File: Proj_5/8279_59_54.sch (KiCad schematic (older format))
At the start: 40 parts, among them SW10 Switch_SW_SPST, SW11 Switch_SW_SPST, SW12 Switch_SW_SPST, SW13 Switch_SW_SPST, SW14 Switch_SW_SPST, SW15 Switch_SW_SPST, SW16 Switch_SW_SPST, SW17 Switch_SW_SPST, SW18 Switch_SW_SPST, SW19 Switch_SW_SPST, SW2 Shift, SW20 Switch_SW_SPST, SW21 Switch_SW_SPST, SW22 Switch_SW_SPST, SW23 Switch_SW_SPST, SW3 Switch_SW_SPST, SW4 Switch_SW_SPST, SW5 Switch_SW_SPST, SW6 Switch_SW_SPST, SW7 CTRL, SW8 Switch_SW_SPST, SW9 Switch_SW_SPST, U10 8259, U11 8254, U17 pkd8279, U18 74LS138

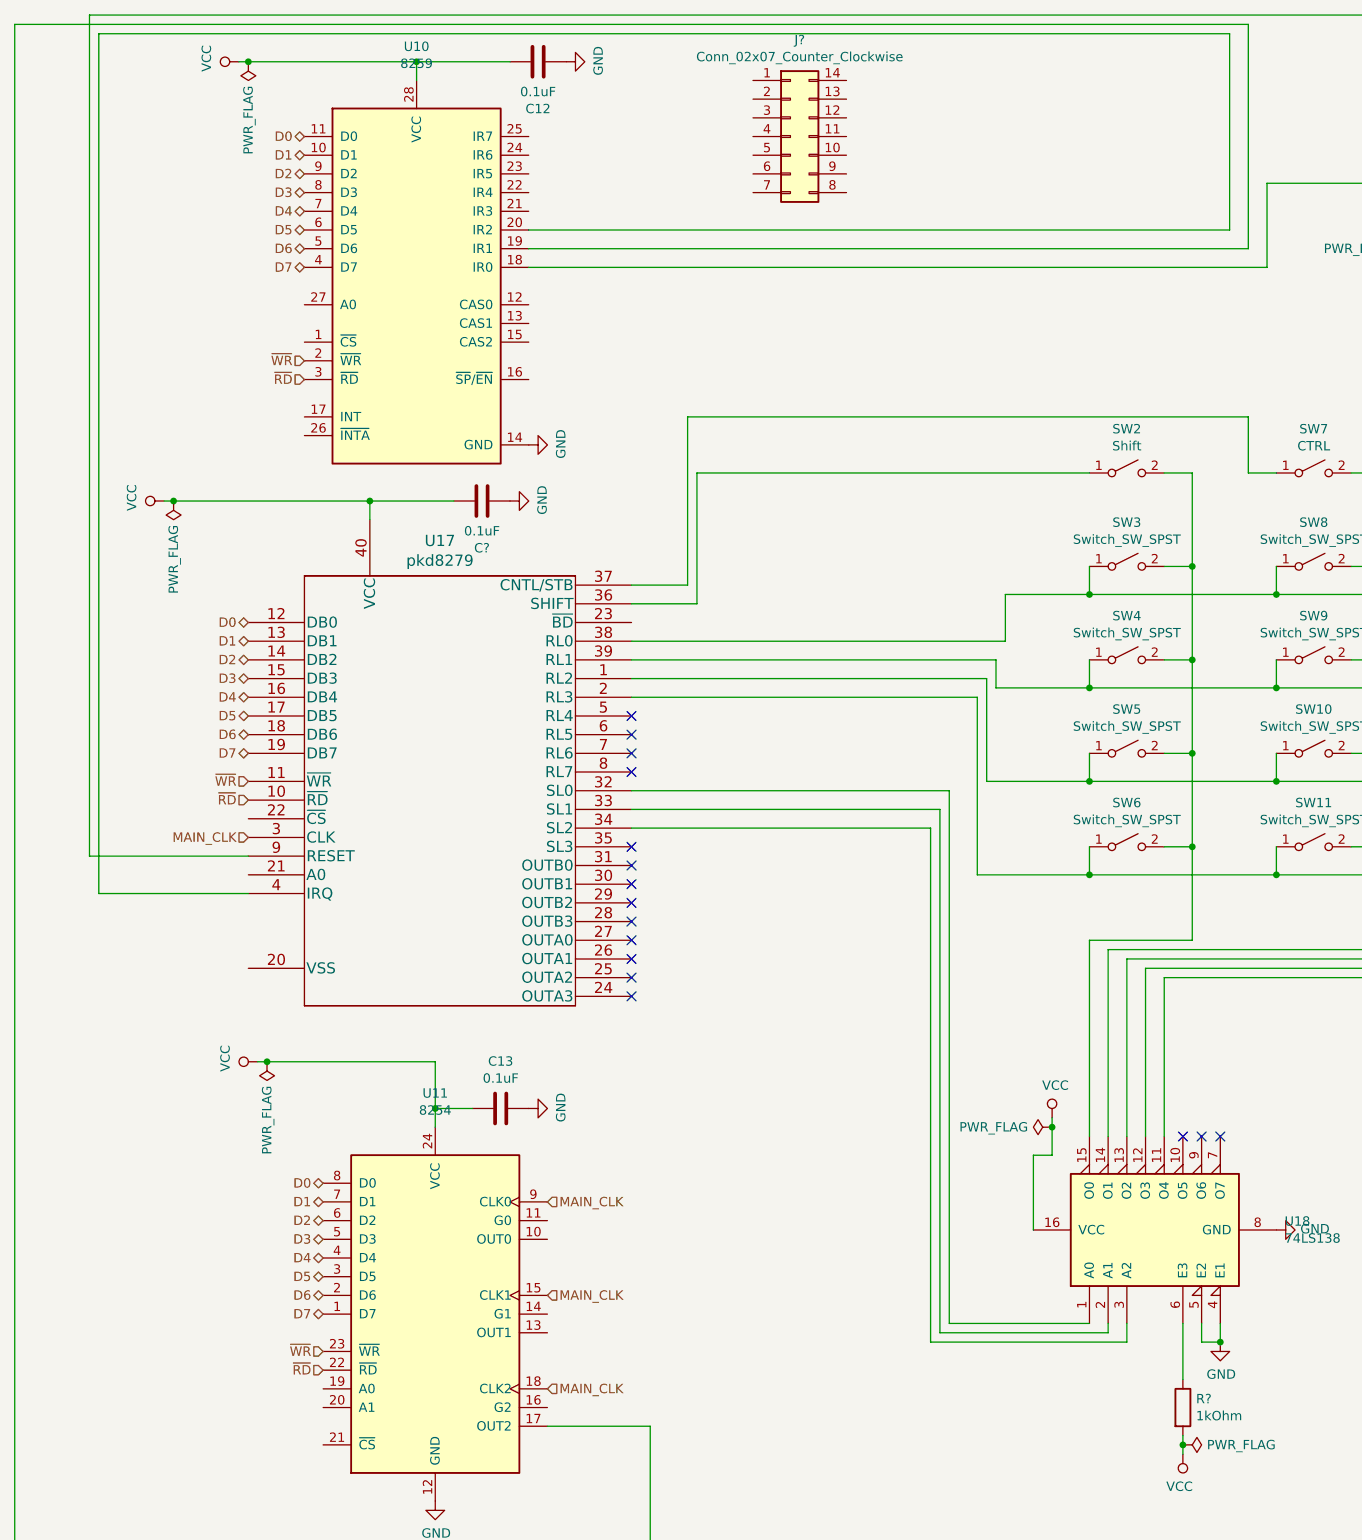
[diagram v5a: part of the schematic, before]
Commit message: Rerouted Ext Wires, UART Mostly Complete, All Headers Added
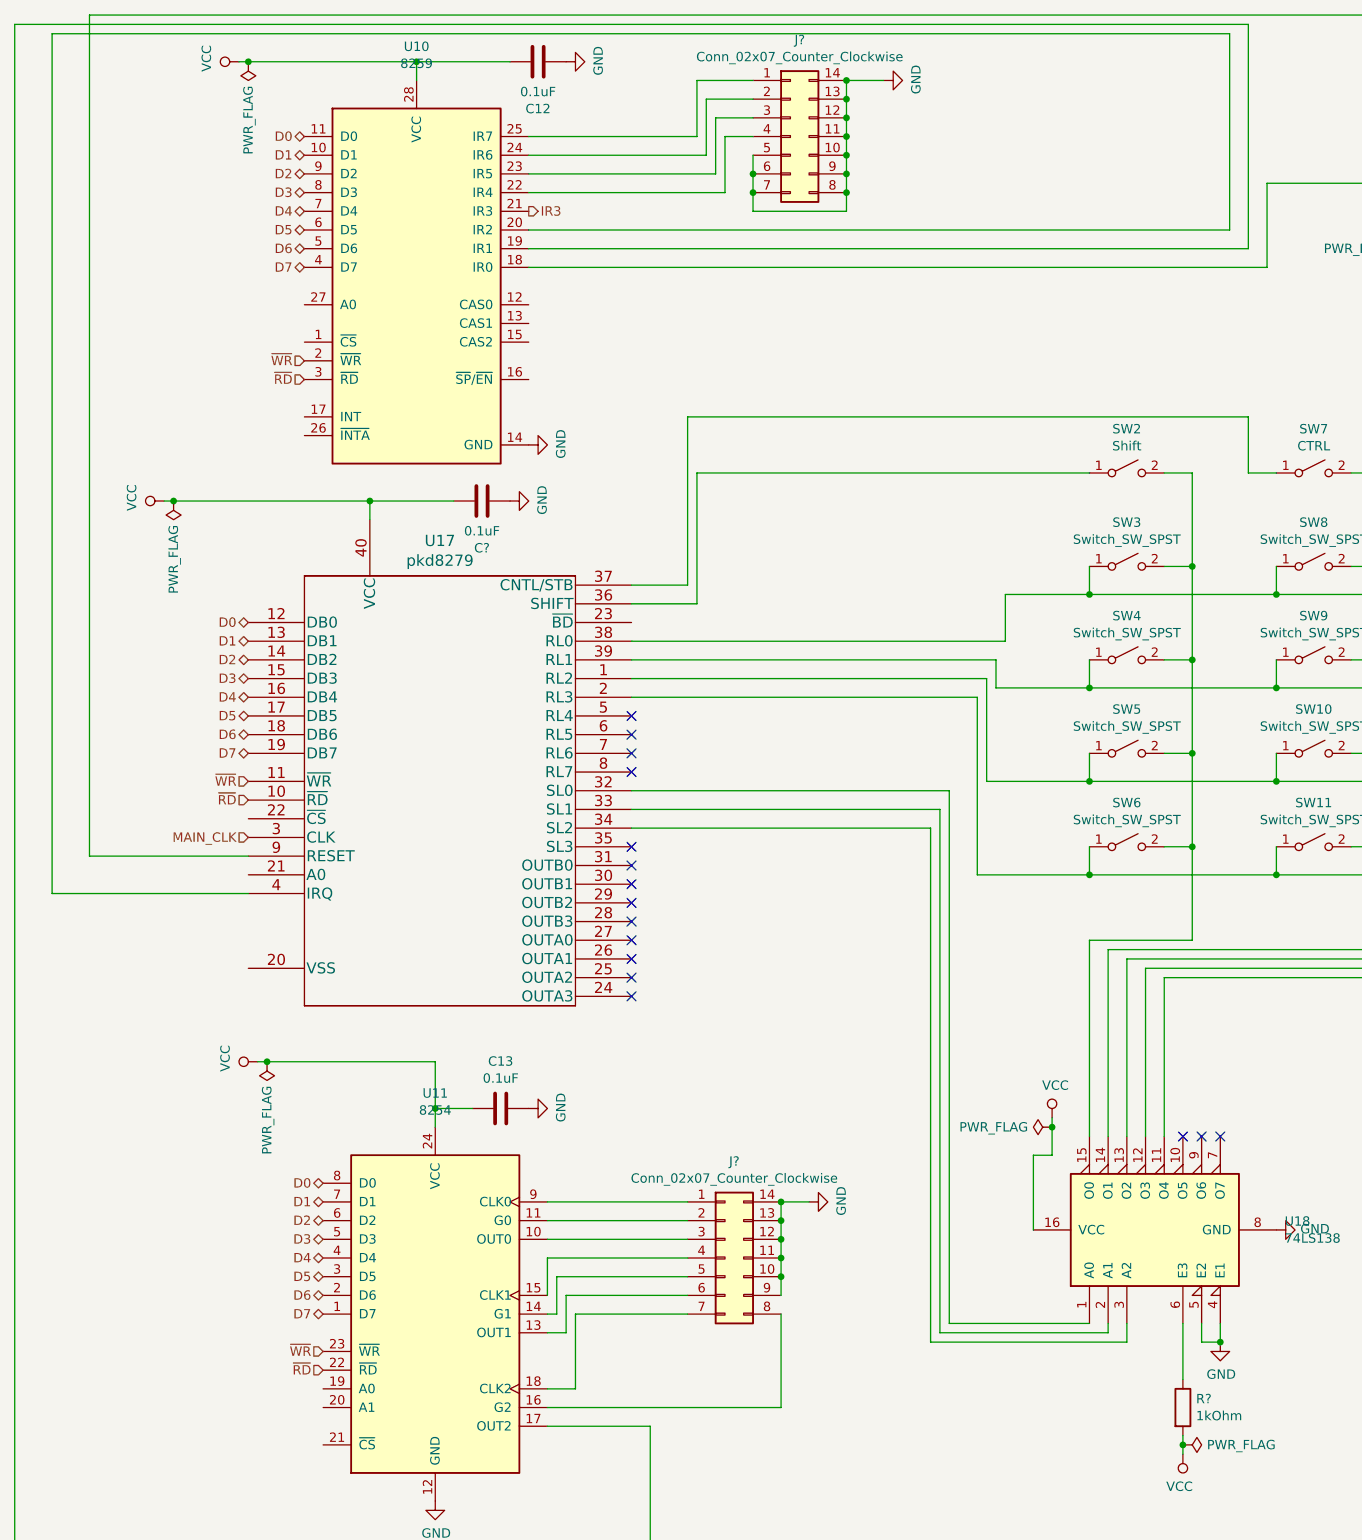
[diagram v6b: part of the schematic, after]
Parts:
- added J?: Conn_02x07_Counter_Clockwise, symbol Connector_Generic:Conn_02x07_Counter_Clockwise
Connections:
- net GND: now also J?.10 (Pin_10), J?.11 (Pin_11), J?.12 (Pin_12), J?.13 (Pin_13), J?.14 (Pin_14), J?.5 (Pin_5), J?.6 (Pin_6), J?.7 (Pin_7), J?.8 (Pin_8), J?.9 (Pin_9), J?.10 (Pin_10), J?.11 (Pin_11), J?.12 (Pin_12), J?.13 (Pin_13), J?.14 (Pin_14), J?.9 (Pin_9)
- net MAIN_CLK: no longer U11.15 (CLK1), U11.18 (CLK2), U11.9 (CLK0)
- net at U11.10 (OUT0): now also J?.3 (Pin_3)
- net at U11.11 (G0): now also J?.2 (Pin_2)
- net at U11.13 (OUT1): now also J?.6 (Pin_6)
- net at U11.14 (G1): now also J?.5 (Pin_5)
- net at U11.16 (G2): now also J?.8 (Pin_8)
- net IR3: now reaches U10.21 (IR3)
- net at U10.22 (IR4): now also J?.4 (Pin_4)
- net at U10.23 (IR5): now also J?.3 (Pin_3)
- net at U10.24 (IR6): now also J?.2 (Pin_2)
- net at U10.25 (IR7): now also J?.1 (Pin_1)
- new net: J?.4 (Pin_4), U11.15 (CLK1)
- new net: J?.7 (Pin_7), U11.18 (CLK2)
- new net: J?.1 (Pin_1), U11.9 (CLK0)
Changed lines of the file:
@@
 $Descr A2 23386 16535
 encoding utf-8
-Sheet 8 9
+Sheet 7 9
 Title ""
 Date ""
@@
 Wire Wire Line
 	11000 1900 7050 1900
-Text HLabel 7150 6900 2    50   Input ~ 0
-MAIN_CLK
 Wire Wire Line
 	15550 1800 15550 1450
@@
 Text HLabel 5550 4950 0    50   Input ~ 0
 MAIN_CLK
-Text HLabel 7150 7400 2    50   Input ~ 0
-MAIN_CLK
-Text HLabel 7150 7900 2    50   Input ~ 0
-MAIN_CLK
 Text HLabel 5850 2400 0    50   Input ~ 0
 ~WR
@@
 	10900 600  10900 1800
 Wire Wire Line
-	4700 550  4700 5050
-Wire Wire Line
 	7050 1700 10800 1700
 Wire Wire Line
 	10800 1700 10800 650
-Wire Wire Line
-	10800 650  4750 650
-Wire Wire Line
-	4750 650  4750 5250
-Wire Wire Line
-	4750 5250 5550 5250
 Wire Wire Line
 	7600 4700 9300 4700
@@
 	1    0    0    -1
 $EndComp
+Text HLabel 7050 1600 2    50   Output ~ 0
+IR3
+Wire Wire Line
+	7050 1200 7950 1200
+Wire Wire Line
+	7950 1200 7950 900
+Wire Wire Line
+	7950 900  8250 900
+Wire Wire Line
+	7050 1300 8000 1300
+Wire Wire Line
+	8000 1300 8000 1000
+Wire Wire Line
+	8000 1000 8250 1000
+Wire Wire Line
+	7050 1400 8050 1400
+Wire Wire Line
+	8050 1400 8050 1100
+Wire Wire Line
+	8050 1100 8250 1100
+Wire Wire Line
+	7050 1500 8100 1500
+Wire Wire Line
+	8100 1500 8100 1200
+Wire Wire Line
+	8100 1200 8250 1200
+Wire Wire Line
+	8250 1300 8250 1400
+Wire Wire Line
+	8250 1400 8250 1500
+Connection ~ 8250 1400
+Wire Wire Line
+	8250 1500 8250 1600
+Wire Wire Line
+	8250 1600 8750 1600
+Wire Wire Line
+	8750 1600 8750 1500
+Connection ~ 8250 1500
+Connection ~ 8750 1000
+Wire Wire Line
+	8750 1000 8750 900
+Connection ~ 8750 1100
+Wire Wire Line
+	8750 1100 8750 1000
+Connection ~ 8750 1200
+Wire Wire Line
+	8750 1200 8750 1100
+Connection ~ 8750 1300
+Wire Wire Line
+	8750 1300 8750 1200
+Connection ~ 8750 1400
+Wire Wire Line
+	8750 1400 8750 1300
+Connection ~ 8750 1500
+Wire Wire Line
+	8750 1500 8750 1400
+Wire Wire Line
+	8750 900  8950 900
+Connection ~ 8750 900
+$Comp
+L power:GND #PWR?
+U 1 1 5F5C47E7
+P 8950 900
+F 0 "#PWR?" H 8950 650 50  0001 C CNN
+F 1 "GND" H 8955 727 50  0000 C CNN
+F 2 "" H 8950 900 50  0001 C CNN
+F 3 "" H 8950 900 50  0001 C CNN
+	1    8950 900
+	0    -1   -1   0
+$EndComp
+Wire Wire Line
+	4500 650  10800 650
+Wire Wire Line
+	4700 550  4700 5050
+Wire Wire Line
+	4500 650  4500 5250
+Wire Wire Line
+	4500 5250 5550 5250
+$Comp
+L Connector_Generic:Conn_02x07_Counter_Clockwise J?
+U 1 1 5F62591A
+P 8100 7200
+F 0 "J?" H 8150 7717 50  0000 C CNN
+F 1 "Conn_02x07_Counter_Clockwise" H 8150 7626 50  0000 C CNN
+F 2 "" H 8100 7200 50  0001 C CNN
+F 3 "~" H 8100 7200 50  0001 C CNN
+	1    8100 7200
+	1    0    0    -1
+$EndComp
+Wire Wire Line
+	7150 6900 7900 6900
+Wire Wire Line
+	7150 7000 7900 7000
+Wire Wire Line
+	7150 7100 7900 7100
+Wire Wire Line
+	7150 7400 7150 7200
+Wire Wire Line
+	7150 7200 7900 7200
+Wire Wire Line
+	7150 7500 7200 7500
+Wire Wire Line
+	7200 7500 7200 7300
+Wire Wire Line
+	7200 7300 7900 7300
+Wire Wire Line
+	7150 7600 7250 7600
+Wire Wire Line
+	7250 7600 7250 7400
+Wire Wire Line
+	7250 7400 7900 7400
+Wire Wire Line
+	7150 7900 7300 7900
+Wire Wire Line
+	7300 7900 7300 7500
+Wire Wire Line
+	7300 7500 7900 7500
+Wire Wire Line
+	7150 8000 8400 8000
+Wire Wire Line
+	8400 8000 8400 7500
+Wire Wire Line
+	8400 7400 8400 7300
+Connection ~ 8400 7000
+Wire Wire Line
+	8400 7000 8400 6900
+Connection ~ 8400 7100
+Wire Wire Line
+	8400 7100 8400 7000
+Connection ~ 8400 7200
+Wire Wire Line
+	8400 7200 8400 7100
+Connection ~ 8400 7300
+Wire Wire Line
+	8400 7300 8400 7200
+Wire Wire Line
+	8400 6900 8550 6900
+Connection ~ 8400 6900
+$Comp
+L power:GND #PWR?
+U 1 1 5F6F628E
+P 8550 6900
+F 0 "#PWR?" H 8550 6650 50  0001 C CNN
+F 1 "GND" H 8555 6727 50  0000 C CNN
+F 2 "" H 8550 6900 50  0001 C CNN
+F 3 "" H 8550 6900 50  0001 C CNN
+	1    8550 6900
+	0    -1   -1   0
+$EndComp
 $EndSCHEMATC

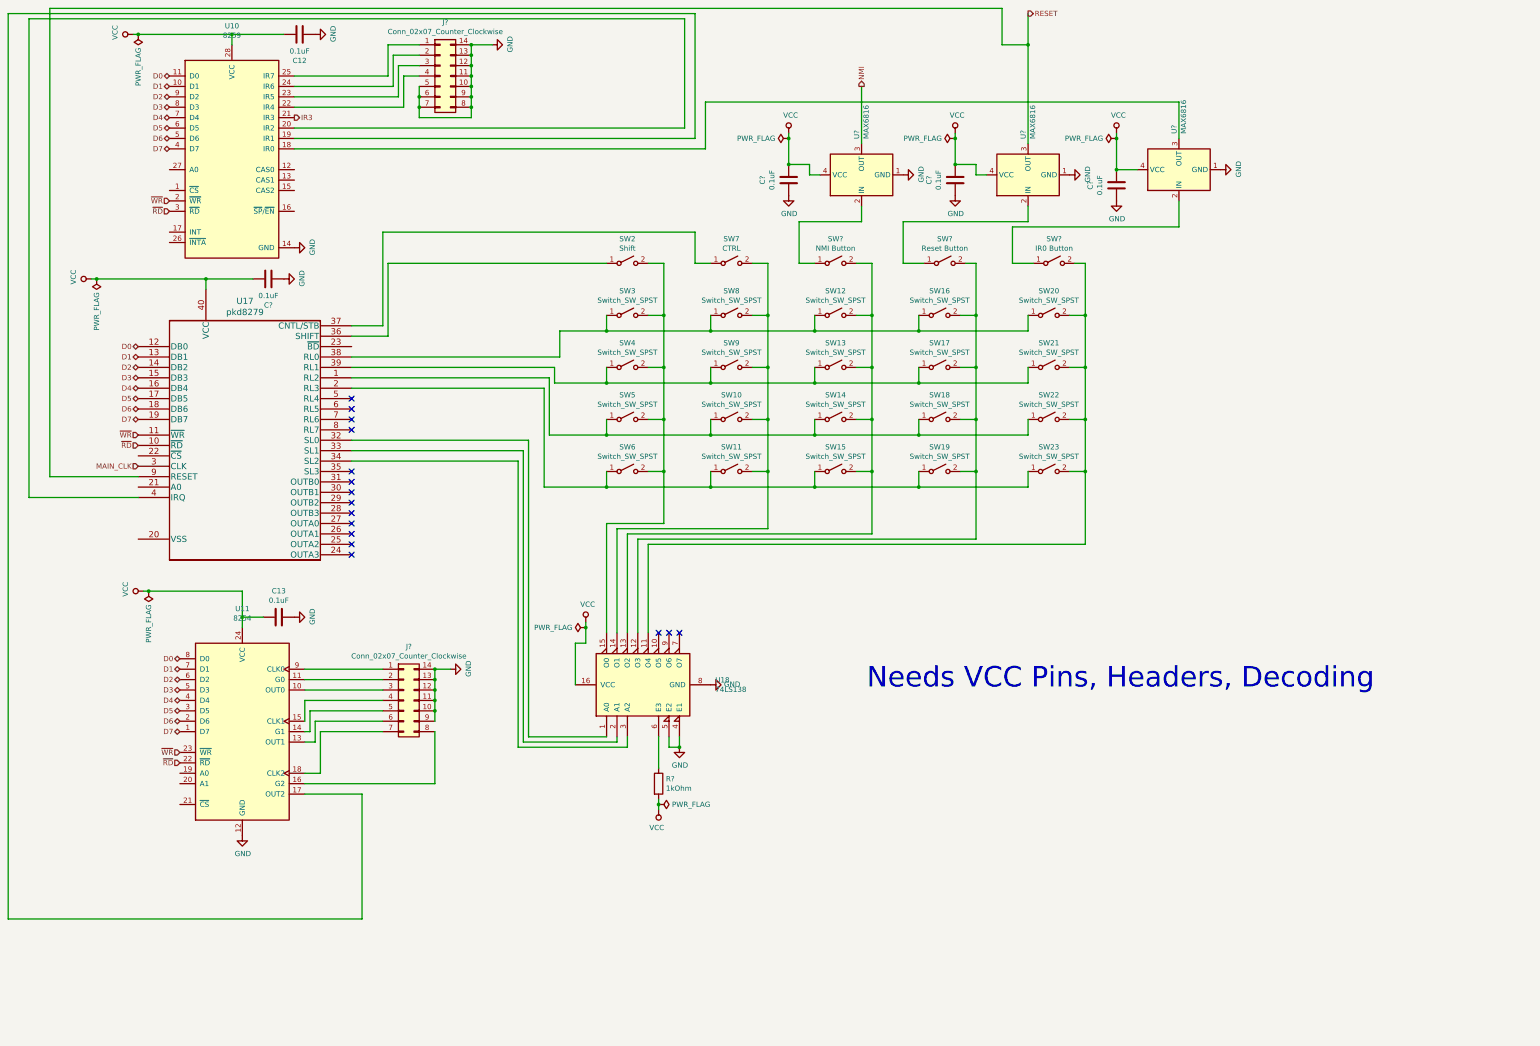
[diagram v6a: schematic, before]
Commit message: Added Power Flags, finished no connects.
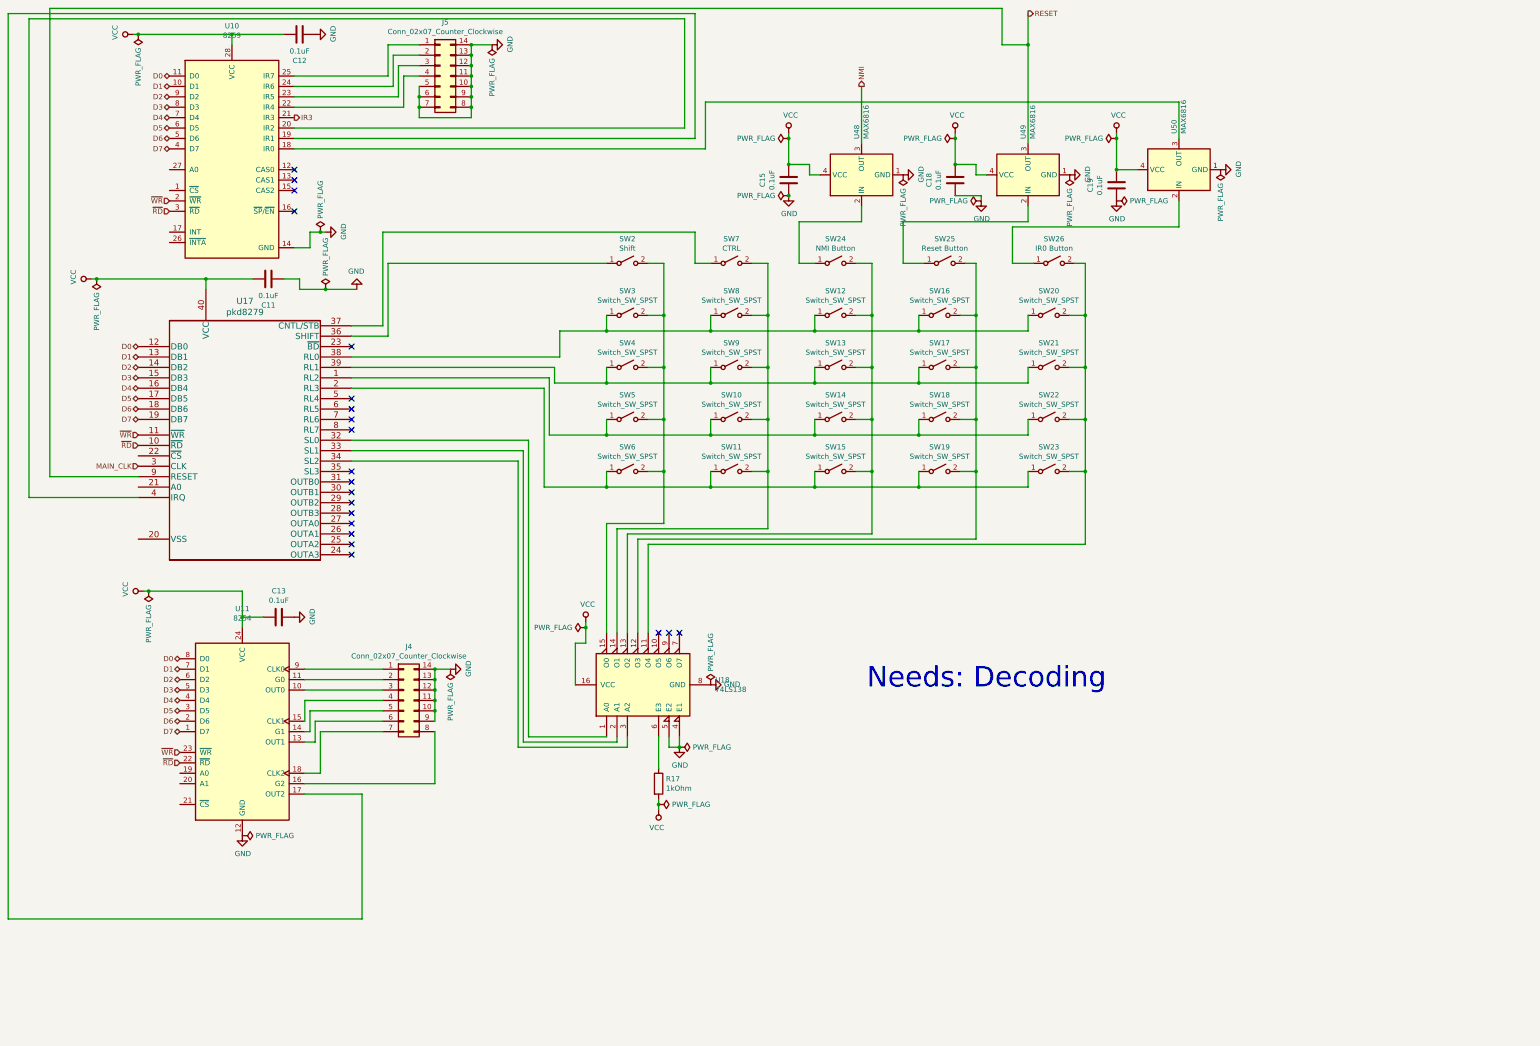
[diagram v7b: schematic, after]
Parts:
- gave numbers to parts that had none: 13
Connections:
- no-connect marks 16 -> 21
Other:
- note added: "Needs: Decoding"
- note removed: "Needs VCC Pins, Headers, Decoding"
